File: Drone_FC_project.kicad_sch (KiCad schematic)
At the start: 1 part, among them U2 STM32F103C8Tx

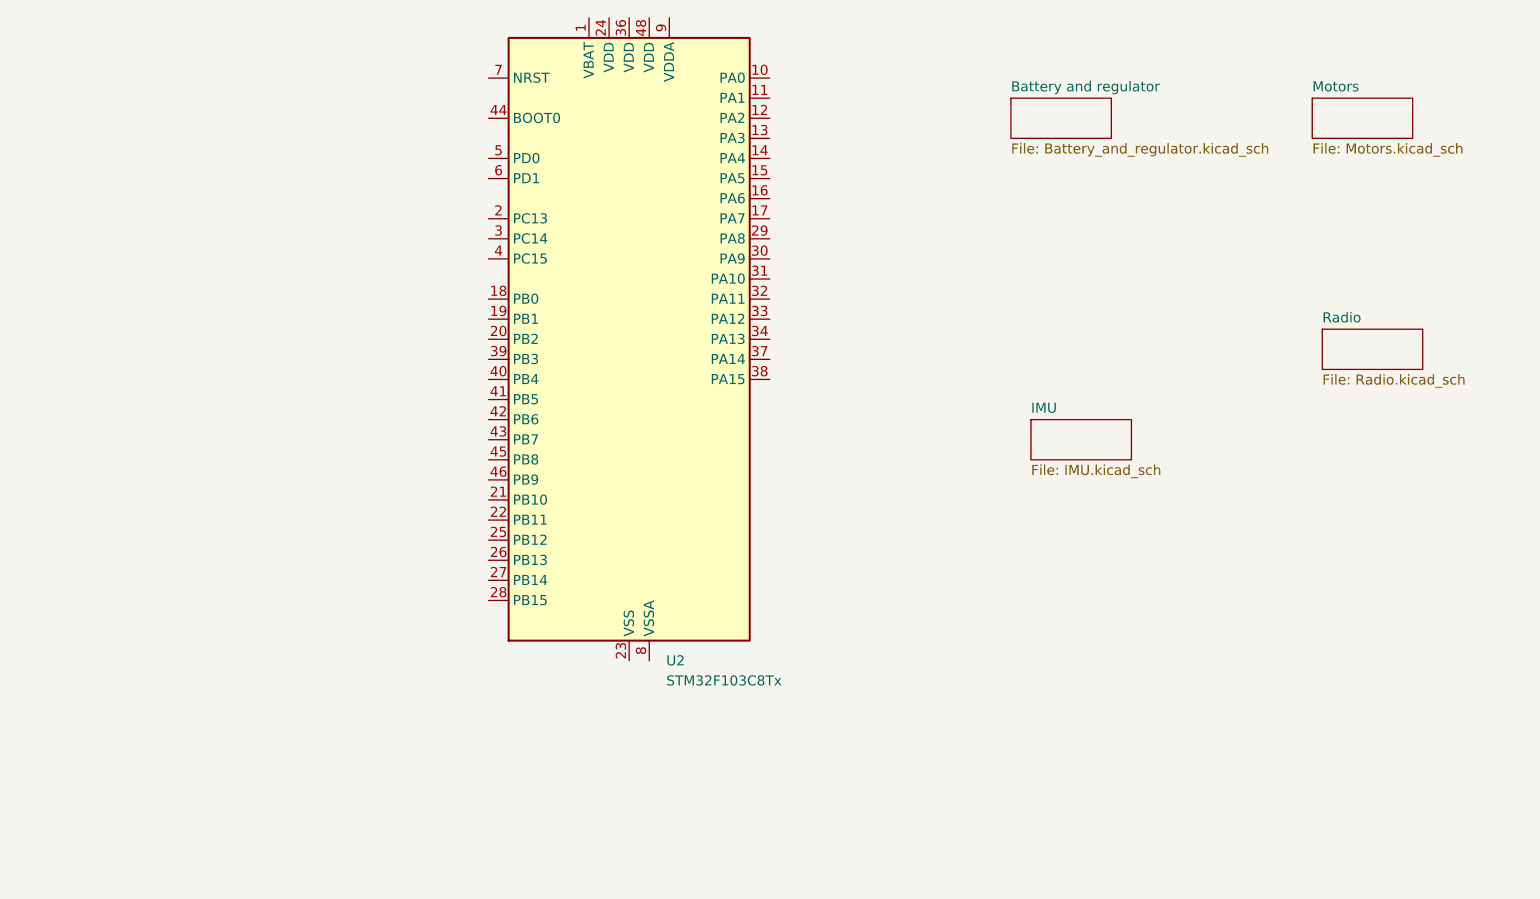
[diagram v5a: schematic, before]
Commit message: Finished motor and battery/regulator subfolders
Also made a folder for holding datasheets.
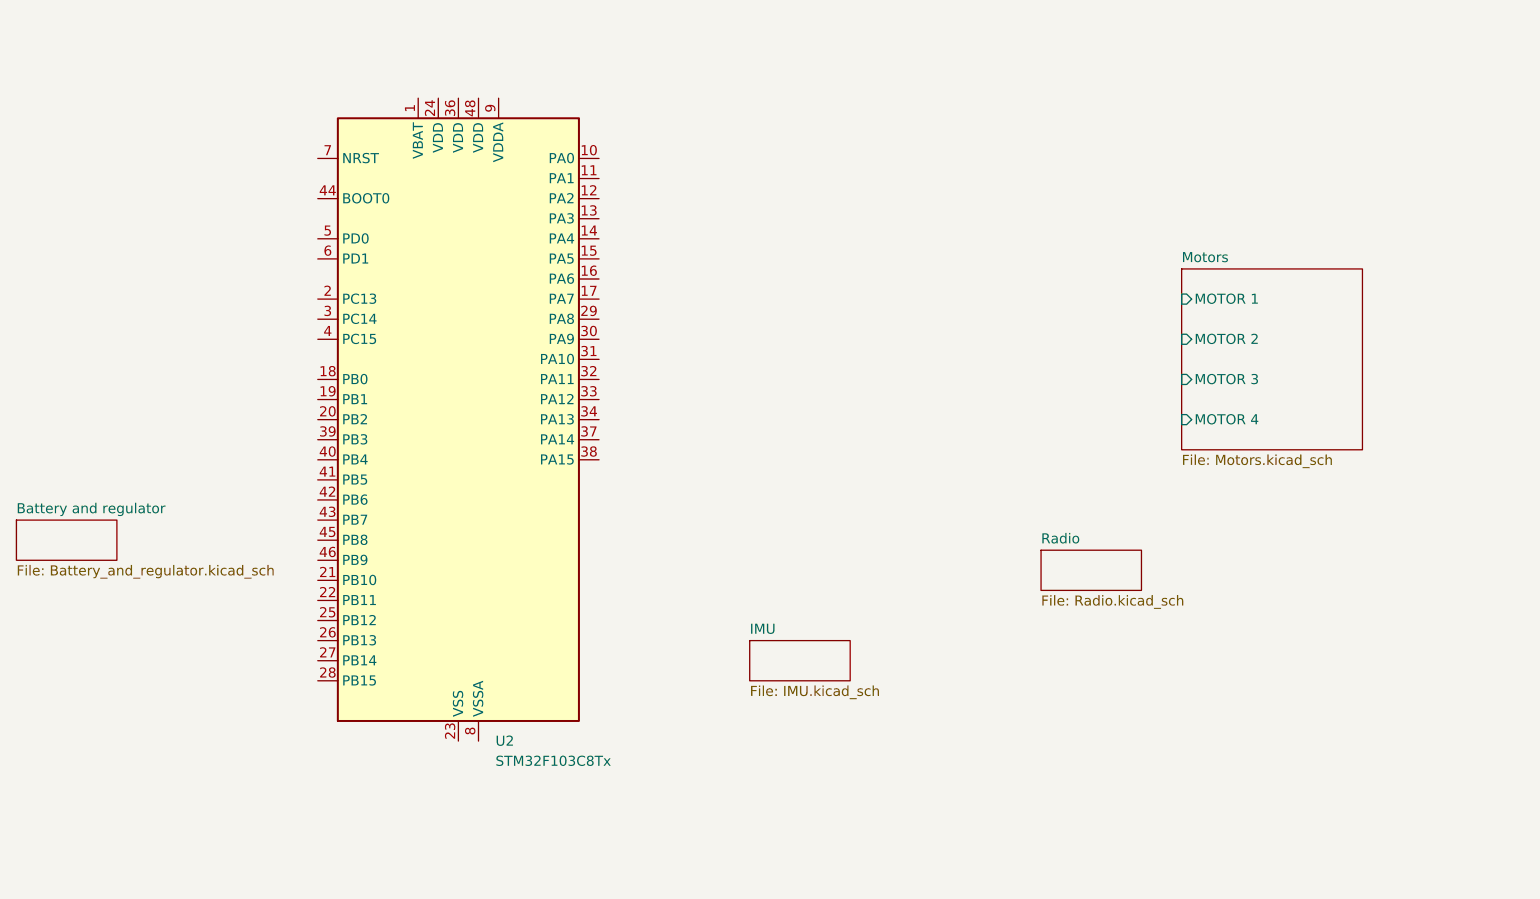
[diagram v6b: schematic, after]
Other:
- sheet Motors ports: added MOTOR 1, MOTOR 2, MOTOR 3, MOTOR 4; removed none
- moved on the sheet: U2
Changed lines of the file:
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@@
 	(symbol
 		(lib_id "MCU_ST_STM32F1:STM32F103C8Tx")
-		(at 128.27 71.12 0)
+		(at 106.68 81.28 0)
 		(unit 1)
 		(body_style 1)
@@
 		(fields_autoplaced yes)
 		(property "Reference" "U2"
-			(at 132.9533 111.76 0)
+			(at 111.3633 121.92 0)
 			(show_name no)
 			(do_not_autoplace no)
@@
 		)
 		(property "Value" "STM32F103C8Tx"
-			(at 132.9533 114.3 0)
+			(at 111.3633 124.46 0)
 			(show_name no)
 			(do_not_autoplace no)
@@
 		)
 		(property "Footprint" "Package_QFP:LQFP-48_7x7mm_P0.5mm"
-			(at 113.03 109.22 0)
+			(at 91.44 119.38 0)
 			(hide yes)
 			(show_name no)
@@
 		)
 		(property "Datasheet" "https://www.st.com/resource/en/datasheet/stm32f103c8.pdf"
-			(at 128.27 71.12 0)
+			(at 106.68 81.28 0)
 			(hide yes)
 			(show_name no)
@@
 		)
 		(property "Description" "STMicroelectronics Arm Cortex-M3 MCU, 64KB flash, 20KB RAM, 72 MHz, 2.0-3.6V, 37 GPIO, LQFP48"
-			(at 128.27 71.12 0)
+			(at 106.68 81.28 0)
 			(hide yes)
 			(show_name no)
@@
 	)
 	(sheet
-		(at 214.63 40.64)
-		(size 12.7 5.08)
+		(at 198.12 62.23)
+		(size 22.86 22.86)
 		(exclude_from_sim no)
 		(in_bom yes)
@@
 		)
 		(property "Sheetname" "Motors"
-			(at 214.63 39.9284 0)
+			(at 198.12 61.5184 0)
 			(show_name no)
 			(do_not_autoplace no)
@@
 		)
 		(property "Sheetfile" "Motors.kicad_sch"
-			(at 214.63 46.3046 0)
+			(at 198.12 85.6746 0)
 			(show_name no)
 			(do_not_autoplace no)
@@
 				)
 				(justify left top)
+			)
+		)
+		(pin "MOTOR 1" input
+			(at 198.12 66.04 180)
+			(effects
+				(font
+					(size 1.27 1.27)
+				)
+				(justify left)
+			)
+		)
+		(pin "MOTOR 2" input
+			(at 198.12 71.12 180)
+			(effects
+				(font
+					(size 1.27 1.27)
+				)
+				(justify left)
+			)
+		)
+		(pin "MOTOR 3" input
+			(at 198.12 76.2 180)
+			(effects
+				(font
+					(size 1.27 1.27)
+				)
+				(justify left)
+			)
+		)
+		(pin "MOTOR 4" input
+			(at 198.12 81.28 180)
+			(effects
+				(font
+					(size 1.27 1.27)
+				)
+				(justify left)
 			)
 		)
@@
 	)
 	(sheet
-		(at 176.53 40.64)
+		(at 50.8 93.98)
 		(size 12.7 5.08)
 		(exclude_from_sim no)
@@
 		)
 		(property "Sheetname" "Battery and regulator"
-			(at 176.53 39.9284 0)
+			(at 50.8 93.2684 0)
 			(show_name no)
 			(do_not_autoplace no)
@@
 		)
 		(property "Sheetfile" "Battery_and_regulator.kicad_sch"
-			(at 176.53 46.3046 0)
+			(at 50.8 99.6446 0)
 			(show_name no)
 			(do_not_autoplace no)
@@
 	)
 	(sheet
-		(at 215.9 69.85)
+		(at 180.34 97.79)
 		(size 12.7 5.08)
 		(exclude_from_sim no)
@@
 		)
 		(property "Sheetname" "Radio"
-			(at 215.9 69.1384 0)
+			(at 180.34 97.0784 0)
 			(show_name no)
 			(do_not_autoplace no)
@@
 		)
 		(property "Sheetfile" "Radio.kicad_sch"
-			(at 215.9 75.5146 0)
+			(at 180.34 103.4546 0)
 			(show_name no)
 			(do_not_autoplace no)
@@
 	)
 	(sheet
-		(at 179.07 81.28)
+		(at 143.51 109.22)
 		(size 12.7 5.08)
 		(exclude_from_sim no)
@@
 		)
 		(property "Sheetname" "IMU"
-			(at 179.07 80.5684 0)
+			(at 143.51 108.5084 0)
 			(show_name no)
 			(do_not_autoplace no)
@@
 		)
 		(property "Sheetfile" "IMU.kicad_sch"
-			(at 179.07 86.9446 0)
-			(show_name no)
-			(do_not_autoplace no)
+			(at 143.51 114.8846 0)
+			(show_name no)
+			(do_not_autoplace no)
